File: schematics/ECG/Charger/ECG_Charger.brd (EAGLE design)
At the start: 11.6 x 27.7 mm, 10 parts, among them IC1 MCP73832_SOT23-5

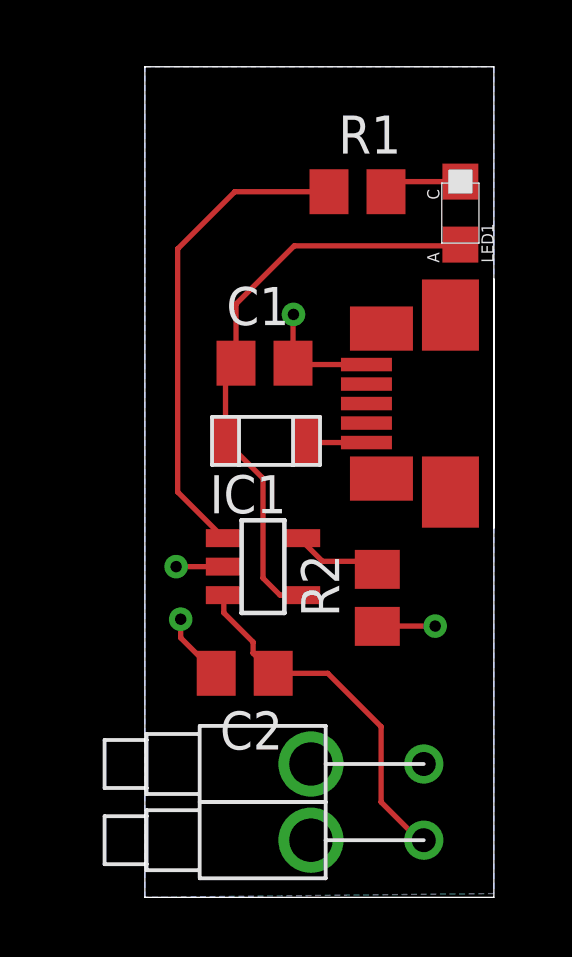
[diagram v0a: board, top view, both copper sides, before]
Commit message: changed micro USB port
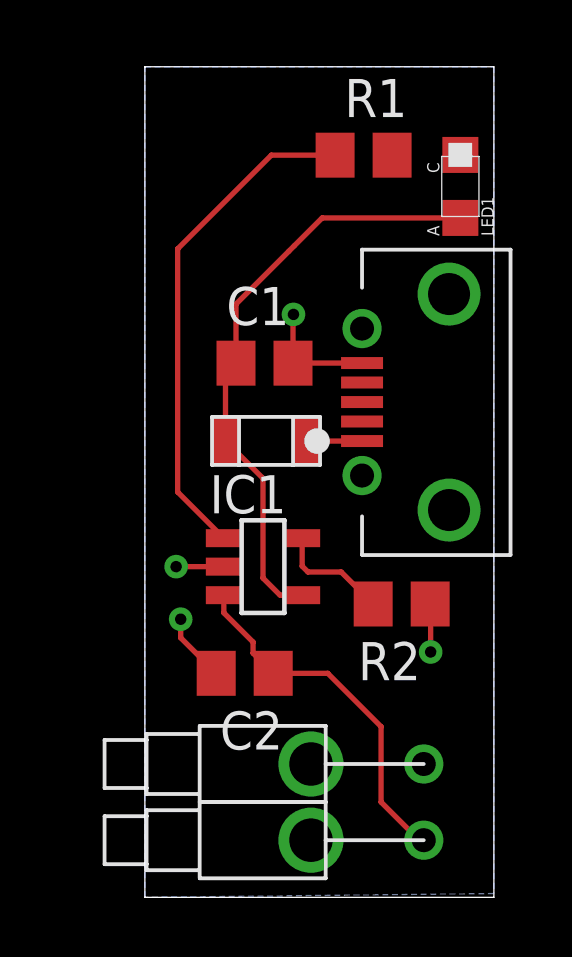
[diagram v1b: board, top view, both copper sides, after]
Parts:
- removed USBCONN: MOLEX-47346-0001, usb_con-update:MOLEX-47364-0001
- added J1: USB_MICROC, KomodoOpenLab:USB_MICROB_FEMALE_RA_SMT
- moved R1 1.24 mm to (7.29, 24.7)
- moved LED1 0.89 mm to (10.5, 23.6)
- moved R2 0.84 mm to (8.56, 9.78), turned to 180 degrees
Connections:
- net GND: now also J1.P$5; no longer USBCONN.5
- net VUSB_5V: now also J1.P$1; no longer USBCONN.1
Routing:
- net N$3: track 2.62 -> 0.00 mm
- net VPROG: track 2.99 -> 3.82 mm
- net STAT: track 16.1 -> 16.8 mm
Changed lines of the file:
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@@
 <elements>
 <element name="IC1" library="KomodoOpenLab" package="SOT23-5" value="MCP73832_SOT23-5" x="3.937" y="11.0236" rot="R270"/>
-<element name="R2" library="rcl" package="R0805" value="10K" x="7.747" y="9.9822" rot="R90"/>
+<element name="R2" library="rcl" package="R0805" value="10K" x="8.5598" y="9.779" rot="R180"/>
 <element name="C1" library="rcl" package="C0805" value="4.7uF" x="3.9878" y="17.8054"/>
-<element name="LED1" library="LITEON" package="SMT_LED_0805" value="LED_SMT_0805" x="10.5156" y="22.7584" rot="R90"/>
-<element name="R1" library="rcl" package="R0805" value="470" x="7.0866" y="23.5204"/>
-<element name="USBCONN" library="usb_con-update" package="MOLEX-47364-0001" value="MOLEX-47346-0001" x="10.1854" y="16.4592" rot="R180"/>
+<element name="LED1" library="LITEON" package="SMT_LED_0805" value="LED_SMT_0805" x="10.5156" y="23.6474" rot="R90"/>
+<element name="R1" library="rcl" package="R0805" value="470" x="7.2898" y="24.7396"/>
 <element name="FUSE" library="bourns-fuse" package="1206" value="FUSE-MF_SERIES" x="4.0386" y="15.2146" rot="R180"/>
 <element name="C2" library="rcl" package="C0805" value="4.7uF" x="3.3274" y="7.4676" rot="R180"/>
 <element name="U$1" library="pins" package="PISTON_RA_TH" value="PISTON_RA_TH" x="9.2964" y="1.905" rot="R180"/>
 <element name="U$2" library="pins" package="PISTON_RA_TH" value="PISTON_RA_TH" x="9.2964" y="4.445" rot="R180"/>
+<element name="J1" library="KomodoOpenLab" package="USB_MICROB_FEMALE_RA_SMT" value="USB_MICROC" x="9.779" y="16.51" rot="R90">
+<attribute name="DIGIKEY" value="WM1399CT-ND" x="9.779" y="16.51" size="1.778" layer="27" rot="R90" display="off"/>
+<attribute name="PN" value="ZX62D-B-5PA8" x="9.779" y="16.51" size="1.778" layer="27" rot="R90" display="off"/>
+</element>
 </elements>
 <signals>
@@
 <contactref element="C1" pad="2"/>
 <contactref element="IC1" pad="2"/>
-<contactref element="USBCONN" pad="5"/>
 <contactref element="C2" pad="2"/>
 <contactref element="R2" pad="1"/>
@@
 <vertex x="0" y="0"/>
 </polygon>
-<via x="9.6774" y="9.0424" extent="1-16" drill="0.381"/>
+<via x="9.525" y="8.1788" extent="1-16" drill="0.381"/>
 <via x="4.953" y="19.431" extent="1-16" drill="0.381"/>
-<wire x1="7.3854" y1="17.7592" x2="4.9378" y2="17.7592" width="0.1778" layer="1"/>
 <wire x1="4.9378" y1="17.7592" x2="4.9378" y2="17.8054" width="0.1778" layer="1"/>
 <wire x1="4.953" y1="19.431" x2="4.9378" y2="19.431" width="0.1778" layer="1"/>
@@
 <wire x1="1.1938" y1="9.271" x2="1.1938" y2="8.6512" width="0.1778" layer="1"/>
 <wire x1="1.1938" y1="8.6512" x2="2.3774" y2="7.4676" width="0.1778" layer="1"/>
-<wire x1="9.6774" y1="9.0424" x2="7.7572" y2="9.0424" width="0.1778" layer="1"/>
-<wire x1="7.7572" y1="9.0424" x2="7.747" y2="9.0322" width="0.1778" layer="1"/>
+<contactref element="J1" pad="P$5"/>
+<wire x1="7.239" y1="17.81" x2="4.9378" y2="17.81" width="0.1778" layer="1"/>
+<wire x1="4.9378" y1="17.81" x2="4.9378" y2="17.8054" width="0.1778" layer="1"/>
+<wire x1="9.525" y1="8.1788" x2="9.525" y2="9.7638" width="0.1778" layer="1"/>
+<wire x1="9.525" y1="9.7638" x2="9.5098" y2="9.779" width="0.1778" layer="1"/>
 </signal>
 <signal name="STAT">
 <contactref element="IC1" pad="1"/>
 <contactref element="R1" pad="1"/>
-<wire x1="6.1366" y1="23.5204" x2="2.9972" y2="23.5204" width="0.1778" layer="1"/>
-<wire x1="2.9972" y1="23.5204" x2="1.0922" y2="21.6154" width="0.1778" layer="1"/>
+<wire x1="4.2164" y1="24.7396" x2="1.0922" y2="21.6154" width="0.1778" layer="1"/>
 <wire x1="1.0922" y1="21.6154" x2="1.0922" y2="13.5124" width="0.1778" layer="1"/>
 <wire x1="1.0922" y1="13.5124" x2="2.631" y2="11.9736" width="0.1778" layer="1"/>
+<wire x1="6.3398" y1="24.7396" x2="4.2164" y2="24.7396" width="0.1778" layer="1"/>
 </signal>
 <signal name="VPROG">
 <contactref element="IC1" pad="5"/>
 <contactref element="R2" pad="2"/>
-<wire x1="5.243" y1="11.9736" x2="5.243" y2="11.8766" width="0.1778" layer="1"/>
-<wire x1="5.243" y1="11.8766" x2="5.9182" y2="11.2014" width="0.1778" layer="1"/>
-<wire x1="5.9182" y1="11.2014" x2="7.4778" y2="11.2014" width="0.1778" layer="1"/>
-<wire x1="7.4778" y1="11.2014" x2="7.747" y2="10.9322" width="0.1778" layer="1"/>
+<wire x1="5.243" y1="11.9736" x2="5.243" y2="11.0384" width="0.1778" layer="1"/>
+<wire x1="5.243" y1="11.0384" x2="5.4356" y2="10.8458" width="0.1778" layer="1"/>
+<wire x1="5.4356" y1="10.8458" x2="6.543" y2="10.8458" width="0.1778" layer="1"/>
+<wire x1="6.543" y1="10.8458" x2="7.6098" y2="9.779" width="0.1778" layer="1"/>
 </signal>
 <signal name="N$3">
 <contactref element="LED1" pad="C"/>
 <contactref element="R1" pad="2"/>
-<wire x1="10.5156" y1="23.8584" x2="8.3746" y2="23.8584" width="0.1778" layer="1"/>
-<wire x1="8.3746" y1="23.8584" x2="8.0366" y2="23.5204" width="0.1778" layer="1"/>
+<wire x1="8.2398" y1="24.7396" x2="10.5156" y2="24.7474" width="0" layer="19" extent="1-1"/>
 </signal>
 <signal name="VUSB">
@@
 <wire x1="2.6886" y1="17.8054" x2="2.6886" y2="15.2146" width="0.1778" layer="1"/>
 <wire x1="3.0378" y1="17.8054" x2="3.0378" y2="19.7764" width="0.1778" layer="1"/>
-<wire x1="3.0378" y1="19.7764" x2="4.9784" y2="21.717" width="0.1778" layer="1"/>
-<wire x1="4.9784" y1="21.717" x2="10.4742" y2="21.717" width="0.1778" layer="1"/>
-<wire x1="10.4742" y1="21.717" x2="10.5156" y2="21.7584" width="0.1778" layer="1"/>
+<wire x1="3.0378" y1="19.7764" x2="4.8006" y2="21.5392" width="0.1778" layer="1"/>
+<wire x1="4.8006" y1="21.5392" x2="4.9784" y2="21.717" width="0.1778" layer="1"/>
 <wire x1="5.243" y1="10.0736" x2="4.506" y2="10.0736" width="0.1778" layer="1"/>
 <wire x1="4.506" y1="10.0736" x2="3.937" y2="10.6426" width="0.1778" layer="1"/>
 <wire x1="3.937" y1="10.6426" x2="3.937" y2="13.9662" width="0.1778" layer="1"/>
 <wire x1="3.937" y1="13.9662" x2="2.6886" y2="15.2146" width="0.1778" layer="1"/>
+<wire x1="10.5156" y1="22.6474" x2="5.9088" y2="22.6474" width="0.1778" layer="1"/>
+<wire x1="5.9088" y1="22.6474" x2="4.9784" y2="21.717" width="0.1778" layer="1"/>
 </signal>
 <signal name="VUSB_5V">
-<contactref element="USBCONN" pad="1"/>
 <contactref element="FUSE" pad="1"/>
-<wire x1="7.3854" y1="15.1592" x2="5.3886" y2="15.1592" width="0.1778" layer="1"/>
 <wire x1="5.3886" y1="15.1592" x2="5.3886" y2="15.2146" width="0.1778" layer="1"/>
+<contactref element="J1" pad="P$1"/>
+<wire x1="7.239" y1="15.21" x2="5.3886" y2="15.21" width="0.1778" layer="1"/>
+<wire x1="5.3886" y1="15.21" x2="5.3886" y2="15.2146" width="0.1778" layer="1"/>
 </signal>
 <signal name="BATT">

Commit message: shrunk caps and resistors to 0402 package sizes. Added 124k resistor on ID pin of USB
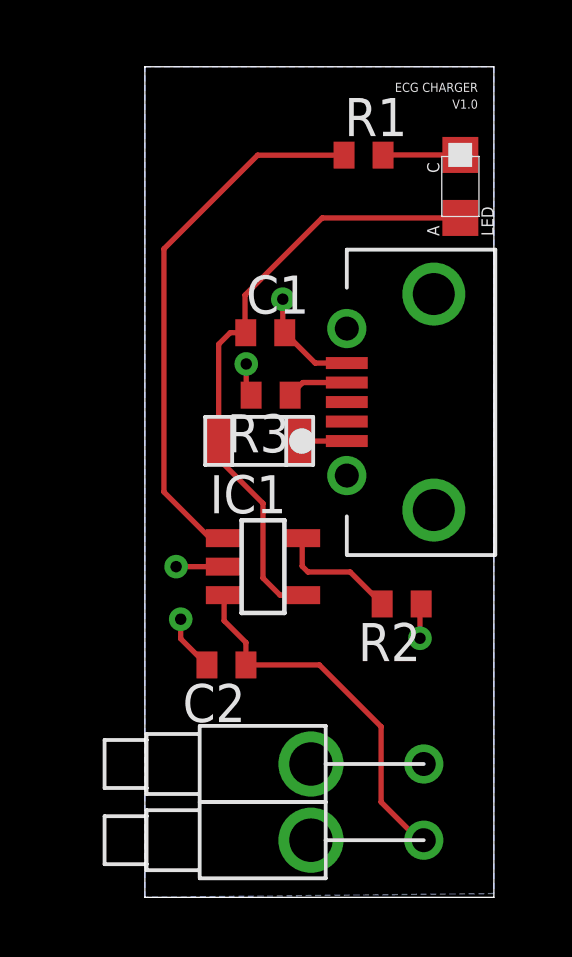
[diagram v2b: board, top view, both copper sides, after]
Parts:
- added R3: 124K, rcl:R0402
- C1, C2: device rcl:C0805 -> rcl:C0402
- R1, R2: device rcl:R0805 -> rcl:R0402
- moved C1 1.02 mm to (4.01, 18.8)
- moved C2 0.67 mm to (2.72, 7.75)
- moved J1 0.51 mm to (9.27, 16.5)
- moved FUSE 0.23 mm to (3.81, 15.2)
- renumbered LED1 to LED
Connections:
- new net N$1: J1.P$4, R3.1
- net GND: now also R3.2
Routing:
- net N$3: track 0.00 -> 2.58 mm
- net N$1: track 0.00 -> 2.06 mm
- net STAT: track 16.8 -> 18.0 mm
- net GND: track 9.48 -> 9.38 mm, vias 4 -> 5
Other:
- board text added: "ECG CHARGER"
- board text added: "V1.0"

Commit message: fixed micro usb name
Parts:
- renumbered J1 to CONN3, U$1 to CONN2, U$2 to CONN1
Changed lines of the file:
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@@
 <?xml version="1.0" encoding="utf-8"?>
 <!DOCTYPE eagle SYSTEM "eagle.dtd">
-<eagle version="6.4">
+<eagle version="6.5.0">
 <drawing>
 <settings>
@@
 <element name="FUSE" library="bourns-fuse" package="1206" value="FUSE-MF_SERIES" x="3.81" y="15.2146" rot="R180"/>
 <element name="C2" library="rcl" package="C0402" value="4.7uF" x="2.7178" y="7.747" rot="R180"/>
-<element name="U$1" library="pins" package="PISTON_RA_TH" value="PISTON_RA_TH" x="9.2964" y="1.905" rot="R180"/>
-<element name="U$2" library="pins" package="PISTON_RA_TH" value="PISTON_RA_TH" x="9.2964" y="4.445" rot="R180"/>
-<element name="J1" library="KomodoOpenLab" package="USB_MICROB_FEMALE_RA_SMT" value="USB_MICROC" x="9.271" y="16.51" rot="R90">
+<element name="CONN2" library="pins" package="PISTON_RA_TH" value="PISTON_RA_TH" x="9.2964" y="1.905" rot="R180"/>
+<element name="CONN1" library="pins" package="PISTON_RA_TH" value="PISTON_RA_TH" x="9.2964" y="4.445" rot="R180"/>
+<element name="CONN3" library="KomodoOpenLab" package="USB_MICROB_FEMALE_RA_SMT" value="USB_MICROC" x="9.271" y="16.51" rot="R90">
 <attribute name="DIGIKEY" value="WM1399CT-ND" x="9.271" y="16.51" size="1.778" layer="27" rot="R90" display="off"/>
 <attribute name="PN" value="ZX62D-B-5PA8" x="9.271" y="16.51" size="1.778" layer="27" rot="R90" display="off"/>
@@
 <contactref element="C2" pad="2"/>
 <contactref element="R2" pad="1"/>
-<contactref element="U$2" pad="1"/>
+<contactref element="CONN1" pad="1"/>
 <polygon width="0.1778" layer="16">
 <vertex x="0" y="27.686"/>
@@
 <via x="1.1938" y="9.271" extent="1-16" drill="0.381"/>
 <wire x1="1.1938" y1="9.271" x2="1.1938" y2="8.621" width="0.1778" layer="1"/>
-<contactref element="J1" pad="P$5"/>
+<contactref element="CONN3" pad="P$5"/>
 <contactref element="R3" pad="2"/>
 <wire x1="1.1938" y1="8.621" x2="2.0678" y2="7.747" width="0.1778" layer="1"/>
@@
 <signal name="VUSB_5V">
 <contactref element="FUSE" pad="1"/>
-<contactref element="J1" pad="P$1"/>
+<contactref element="CONN3" pad="P$1"/>
 <wire x1="6.731" y1="15.21" x2="5.1646" y2="15.21" width="0.1778" layer="1"/>
 <wire x1="5.1646" y1="15.21" x2="5.16" y2="15.2146" width="0.1778" layer="1"/>
@@
 <contactref element="IC1" pad="3"/>
 <contactref element="C2" pad="1"/>
-<contactref element="U$1" pad="1"/>
+<contactref element="CONN2" pad="1"/>
 <wire x1="9.2964" y1="1.905" x2="9.144" y2="1.905" width="0.1778" layer="1"/>
 <wire x1="9.144" y1="1.905" x2="7.874" y2="3.175" width="0.1778" layer="1"/>
@@
 </signal>
 <signal name="N$1">
-<contactref element="J1" pad="P$4"/>
+<contactref element="CONN3" pad="P$4"/>
 <contactref element="R3" pad="1"/>
 <wire x1="6.731" y1="17.16" x2="5.2624" y2="17.16" width="0.1778" layer="1"/>

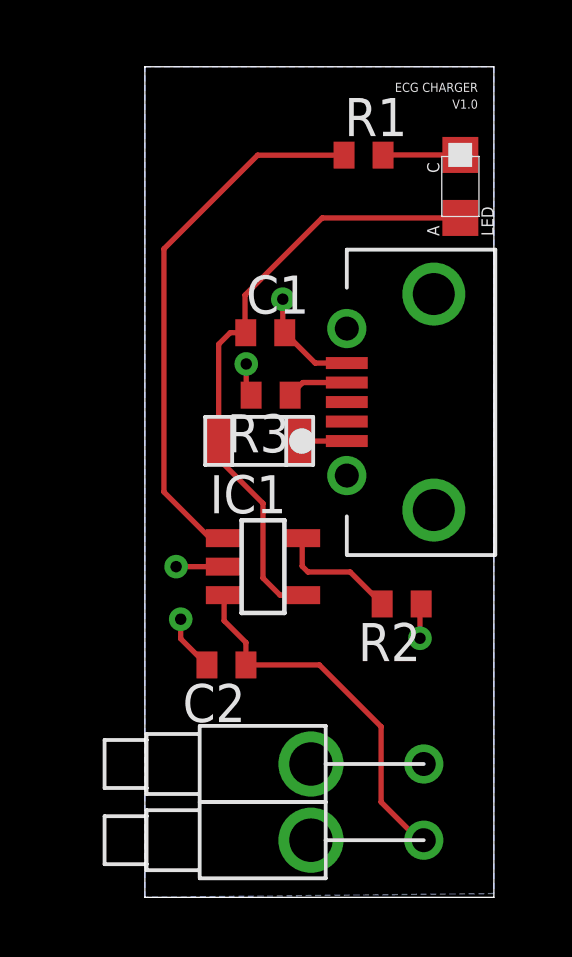
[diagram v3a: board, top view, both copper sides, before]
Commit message: cleaned up the arrangement of the components on the board
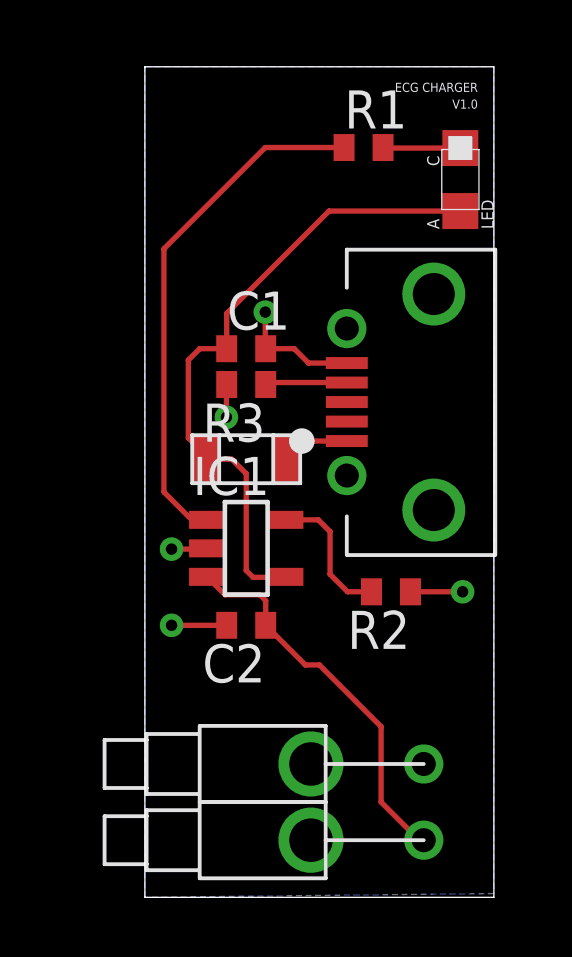
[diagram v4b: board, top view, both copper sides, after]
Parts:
- moved C2 1.48 mm to (3.38, 9.07)
- moved R3 0.89 mm to (3.38, 17.1)
- moved C1 0.83 mm to (3.38, 18.3)
- moved IC1 0.83 mm to (3.38, 11.6)
- moved FUSE 0.75 mm to (3.38, 14.6)
- moved R2 0.54 mm to (8.20, 10.2)
- moved R1 0.25 mm to (7.29, 25.0)
- moved LED 0.23 mm to (10.5, 23.9)
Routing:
- net VUSB: track 20.5 -> 21.5 mm
- net STAT: track 18.0 -> 17.3 mm
- net VUSB_5V: track 1.57 -> 2.25 mm
- net N$1: track 2.06 -> 2.73 mm
- net GND: track 9.38 -> 9.99 mm
- net VPROG: track 4.12 -> 4.70 mm

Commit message: using modified piston package with corrected origin
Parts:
- moved CONN1 5.33 mm to (3.96, 4.45)
- moved CONN2 5.33 mm to (3.96, 1.91)
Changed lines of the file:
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@@
 <element name="FUSE" library="bourns-fuse" package="1206" value="FUSE-MF_SERIES" x="3.3782" y="14.605" rot="R180"/>
 <element name="C2" library="rcl" package="C0402" value="4.7uF" x="3.3782" y="9.0678" rot="R180"/>
-<element name="CONN2" library="pins" package="PISTON_RA_TH" value="PISTON_RA_TH" x="9.2964" y="1.905" rot="R180"/>
-<element name="CONN1" library="pins" package="PISTON_RA_TH" value="PISTON_RA_TH" x="9.2964" y="4.445" rot="R180"/>
+<element name="CONN2" library="pins" package="PISTON_RA_TH" value="PISTON_RA_TH" x="3.9624" y="1.905" rot="R180"/>
+<element name="CONN1" library="pins" package="PISTON_RA_TH" value="PISTON_RA_TH" x="3.9624" y="4.445" rot="R180"/>
 <element name="CONN3" library="KomodoOpenLab" package="USB_MICROB_FEMALE_RA_SMT" value="USB_MICROC" x="9.271" y="16.51" rot="R90">
 <attribute name="DIGIKEY" value="WM1399CT-ND" x="9.271" y="16.51" size="1.778" layer="27" rot="R90" display="off"/>
